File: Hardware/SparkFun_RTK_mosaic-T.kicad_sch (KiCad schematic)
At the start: 51 parts, among them J3 U.FL, J7 Qwiic_Vertical, J8 RP-SMA_Edge, J9 Screw_Cage_3.5mm-10, U1 ESP32-WROVER-IE-N16R8

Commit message: PCB symbol updates
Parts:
- D15: value PESD0402 -> PESD0402
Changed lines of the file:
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@@
 			)
 		)
-		(property "Value" " PESD0402"
+		(property "Value" "PESD0402"
 			(at 39.37 57.15 90)
 			(effects

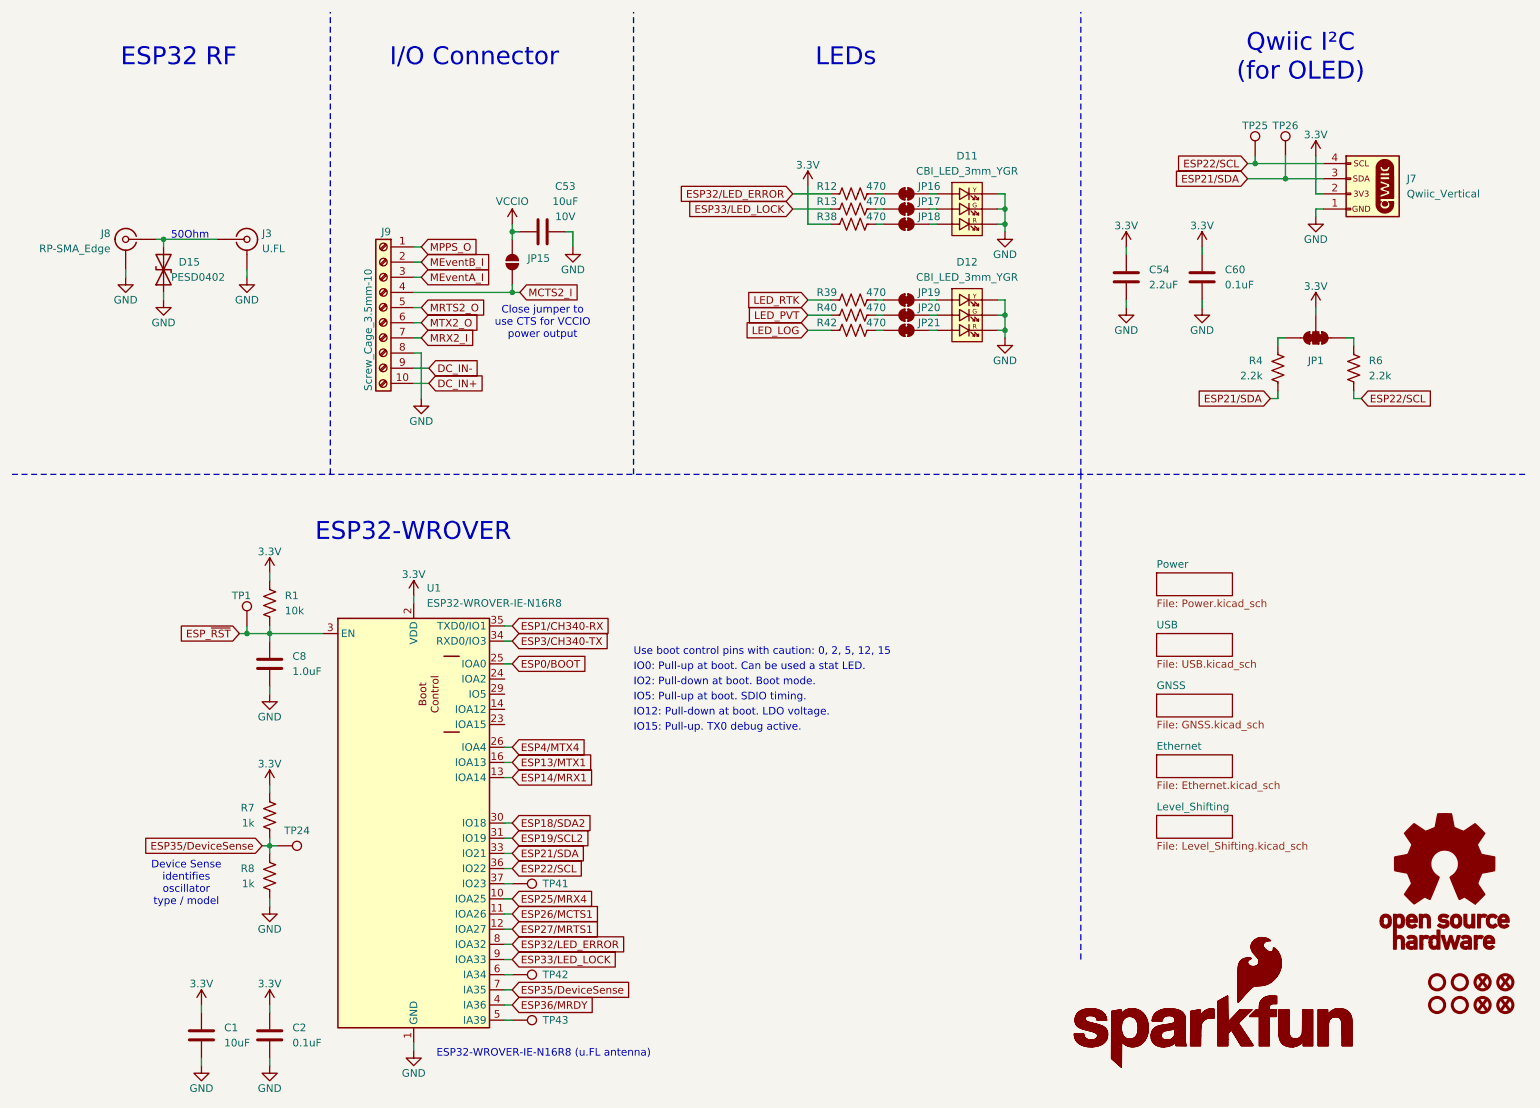
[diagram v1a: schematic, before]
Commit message: Updates for v1.0 PCB
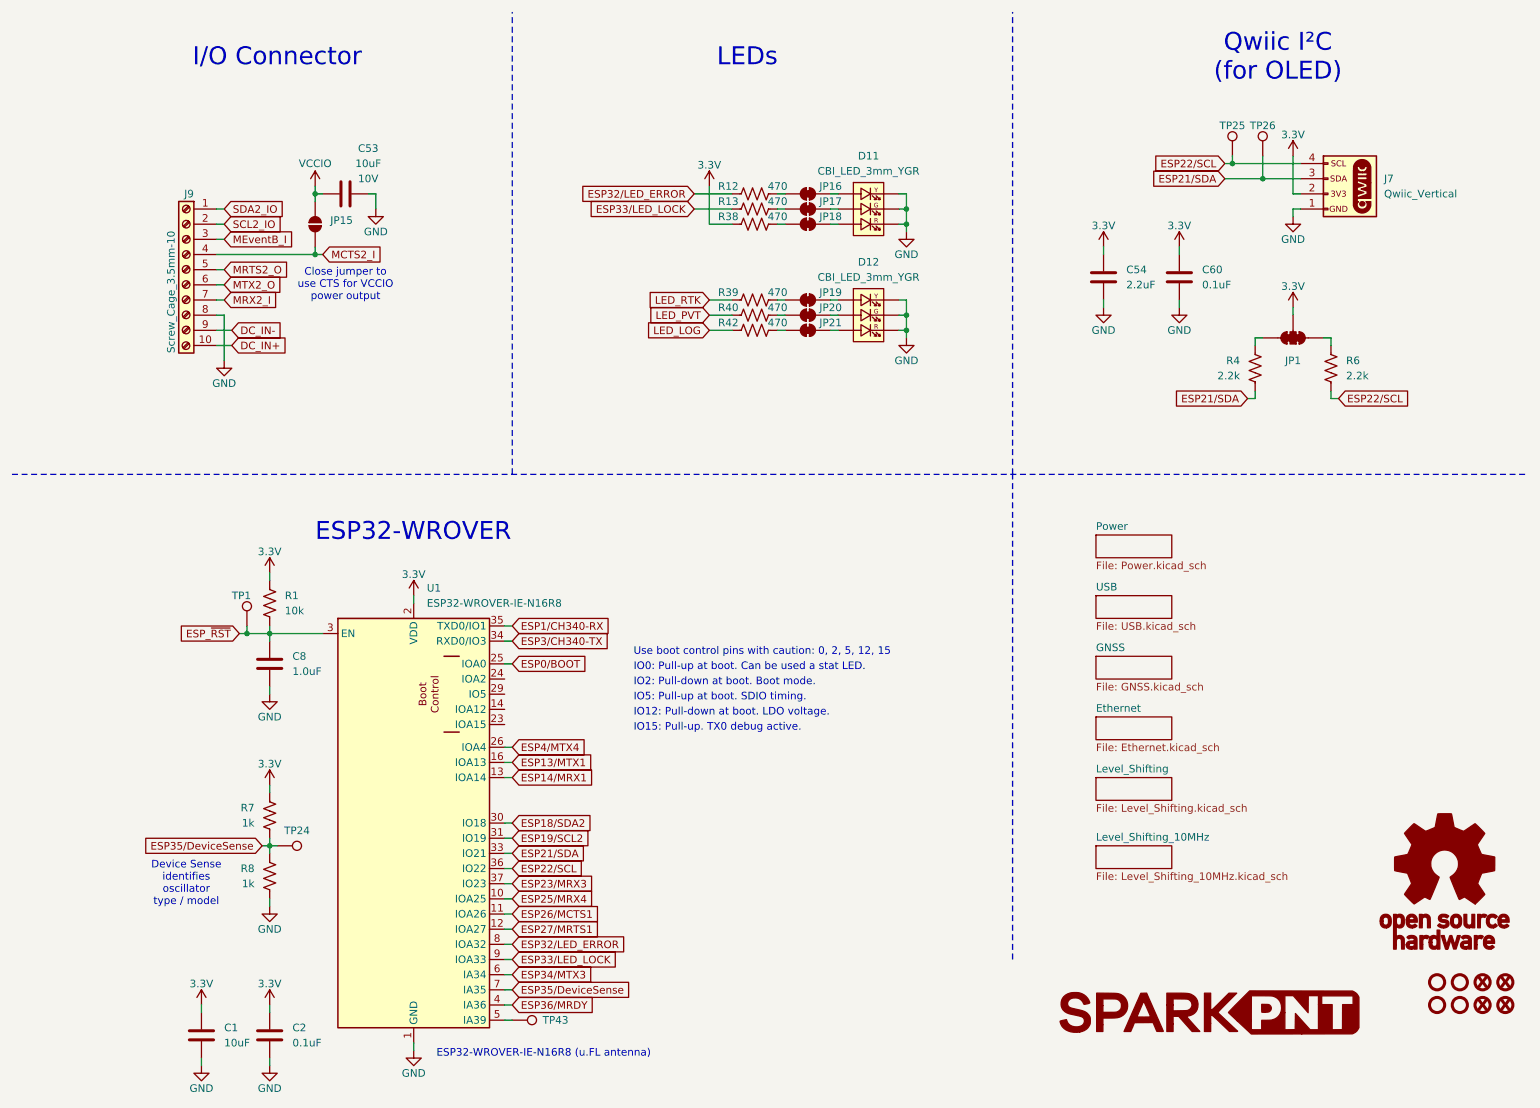
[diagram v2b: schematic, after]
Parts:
- removed D15: PESD0402, SparkFun-Capacitor:C_0402_1005Metric, symbol SparkFun-DiscreteSemi:D_TVS_0402
- removed G3, G5: SparkFun_Logo, symbol SparkFun-Aesthetic:SparkFun_Logo
- removed J3: U.FL, SparkFun-Connector:U.FL, symbol SparkFun-RF:U.FL
- removed J8: RP-SMA_Edge, SparkFun-Connector:RP-SMA_Edge, symbol SparkFun-RF:RP-SMA_EdgeMount
- removed TP41, TP42: PTH, SparkFun-Connector:1x01, symbol SparkFun-Connector:TestPoint_PTH
- added G2: SparkPNT_Logo, symbol SparkFun-Aesthetic:SparkPNT_Logo
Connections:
- net MEventA_I is gone; now on net MEventB_I: J9.3 (Pin_3)
- net MEventB_I: no longer J9.2 (Pin_2)
- net ESP34/MTX3: now reaches U1.6 (IA34)
- net ESP23/MRX3: now reaches U1.37 (IO23)
- net MPPS_O renamed SDA2_IO
- new net SCL2_IO: J9.2 (Pin_2)
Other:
- added sheet Level_Shifting_10MHz (Level_Shifting_10MHz.kicad_sch)
- note removed: "50Ohm"
- note removed: "ESP32 RF"
- title: RTK mosaic-T -> GPSDO (mosaic-T)
- moved on the sheet: C53, C54, C60, D11, D12, J7, J9, JP1, JP15, JP16, JP17, JP18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

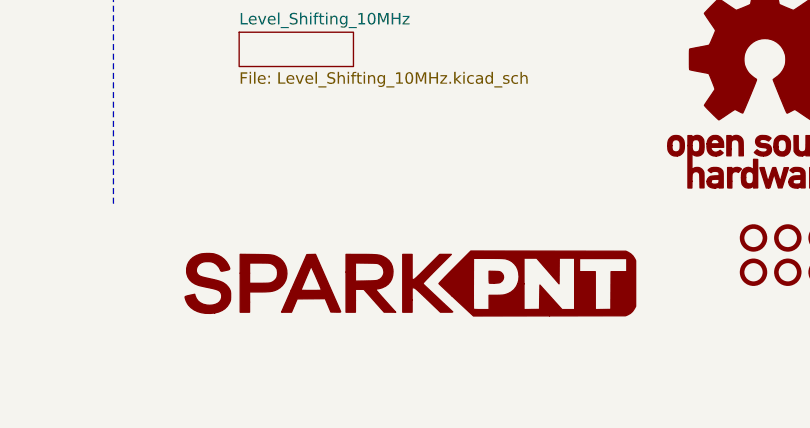
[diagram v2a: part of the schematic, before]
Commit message: Update logo symbol and footprint
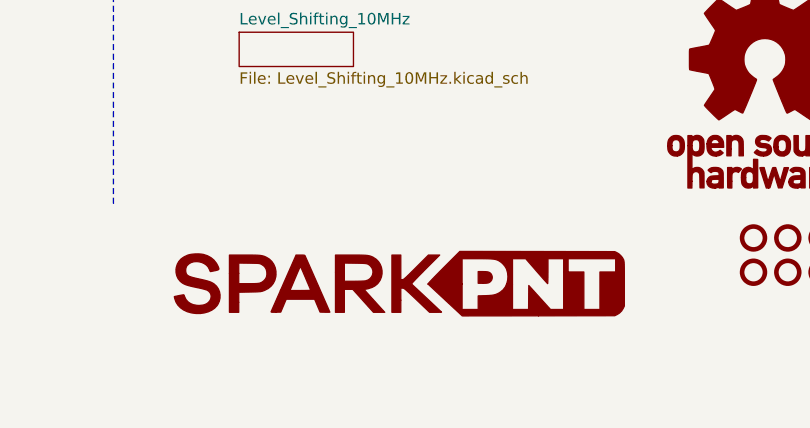
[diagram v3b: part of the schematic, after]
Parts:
- G2: value SparkPNT_Logo -> LOGO
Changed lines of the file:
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@@
+	)
+	(symbol
+		(lib_id "SparkFun-Aesthetic:SparkPNT_Logo")
+		(at 212.09 180.34 0)
+		(unit 1)
+		(exclude_from_sim no)
+		(in_bom yes)
+		(on_board no)
+		(dnp no)
+		(fields_autoplaced yes)
+		(property "Reference" "G2"
+			(at 212.09 175.895 0)
+			(effects
+				(font
+					(size 1.27 1.27)
+				)
+				(hide yes)
+			)
+		)
+		(property "Value" "LOGO"
+			(at 212.09 184.785 0)
+			(effects
+				(font
+					(size 1.27 1.27)
+				)
+				(hide yes)
+			)
+		)
+		(property "Footprint" ""
+			(at 212.09 180.34 0)
+			(effects
+				(font
+					(size 1.27 1.27)
+				)
+				(hide yes)
+			)
+		)
+		(property "Datasheet" ""
+			(at 212.09 180.34 0)
+			(effects
+				(font
+					(size 1.27 1.27)
+				)
+				(hide yes)
+			)
+		)
+		(property "Description" ""
+			(at 212.09 180.34 0)
+			(effects
+				(font
+					(size 1.27 1.27)
+				)
+				(hide yes)
+			)
+		)
+		(instances
+			(project ""
+				(path "/e3dd3ae4-244d-4cba-9cca-5d2abf83f29a"
+					(reference "G2")
+					(unit 1)
+				)
+			)
+		)
 	)
 	(symbol
@@
 					(unit 1)
 				)
-			)
-		)
-	)
-	(symbol
-		(lib_id "SparkFun-Aesthetic:SparkPNT_Logo")
-		(at 213.36 180.34 0)
-		(unit 1)
-		(exclude_from_sim no)
-		(in_bom yes)
-		(on_board no)
-		(dnp no)
-		(fields_autoplaced yes)
-		(property "Reference" "G2"
-			(at 213.36 175.895 0)
-			(effects
-				(font
-					(size 1.27 1.27)
-				)
-				(hide yes)
-			)
-		)
-		(property "Value" "SparkPNT_Logo"
-			(at 213.36 184.785 0)
-			(effects
-				(font
-					(size 1.27 1.27)
-				)
-				(hide yes)
-			)
-		)
-		(property "Footprint" ""
-			(at 213.36 180.34 0)
-			(effects
-				(font
-					(size 1.27 1.27)
-				)
-				(hide yes)
-			)
-		)
-		(property "Datasheet" ""
-			(at 213.36 180.34 0)
-			(effects
-				(font
-					(size 1.27 1.27)
-				)
-				(hide yes)
-			)
-		)
-		(property "Description" ""
-			(at 213.36 180.34 0)
-			(effects
-				(font
-					(size 1.27 1.27)
-				)
-				(hide yes)
-			)
-		)
-		(instances
-			(project ""
-				(path "/e3dd3ae4-244d-4cba-9cca-5d2abf83f29a"
-					(reference "G2")
-					(unit 1)
-				)

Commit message: Add jumpers for 2.8V and 1.8V In / Out
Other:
- title: GPSDO (mosaic-T) -> GPSDO (mosaic-T, SiT5358)
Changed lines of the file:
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@@
 	(paper "USLetter")
 	(title_block
-		(title "GPSDO (mosaic-T)")
+		(title "GPSDO (mosaic-T, SiT5358)")
 		(date "2024-10-17")
 		(rev "v10")

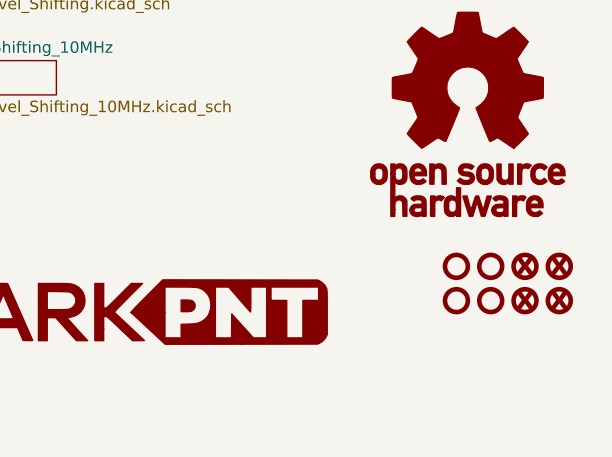
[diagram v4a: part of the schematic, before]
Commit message: Add mounting holes for SiT5811 / Rakon oscillator
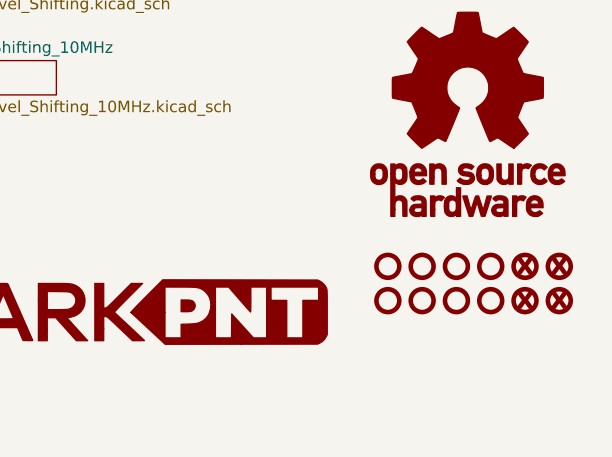
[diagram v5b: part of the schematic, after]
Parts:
- added ST5, ST6, ST7, ST8: Standoff, SparkFun-Hardware:Standoff, symbol SparkFun-Hardware:Standoff
